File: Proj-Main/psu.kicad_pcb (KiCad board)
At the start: 2 copper layers, 100 x 75 mm, 126 parts, among them J1 METER, J3 T1A, J4 T1B, J5 T1C, J6 SENSE, J8 OUT+, J9 OUT-, Q1 BC856, Q10 BC856, Q11 PMP4201Y, Q12 MMBT3904, Q13 BC856, Q14 MMBT3904, Q15 PZT2222A, Q16 MMBT3904, Q17 TIP105, Q18 PMP4201Y, Q19 MMBT2907A, Q2 MMBT3904, Q20 MMBT2907A, Q21 MMBT2907A, Q22 MMBT3904, Q23 PMP4201Y, Q24 MMBT3904, Q3 PZT2222A, Q4 BC856, Q5 MMBT3906, Q6 MMBT3906, Q7 PMP4201Y, Q8 PMP4201Y, Q9 BC856

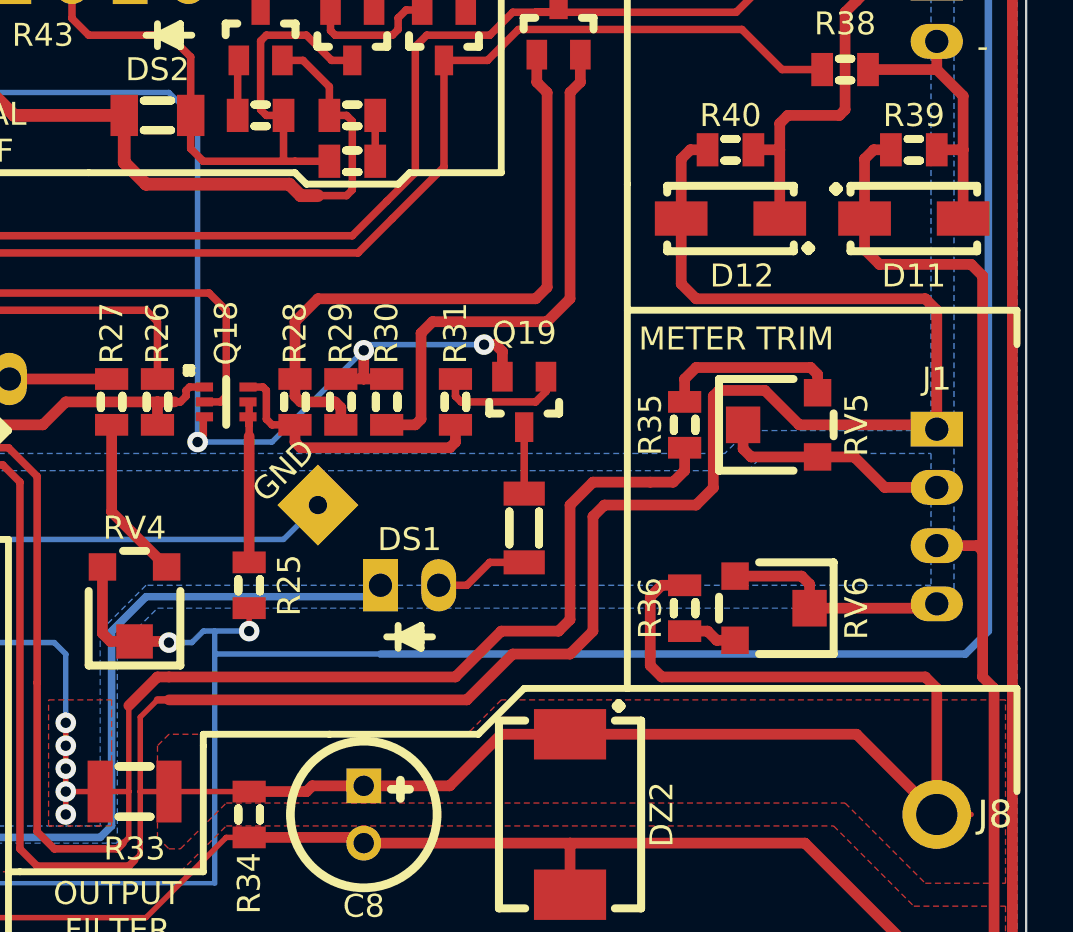
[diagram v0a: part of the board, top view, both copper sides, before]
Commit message: Rearranged schematic
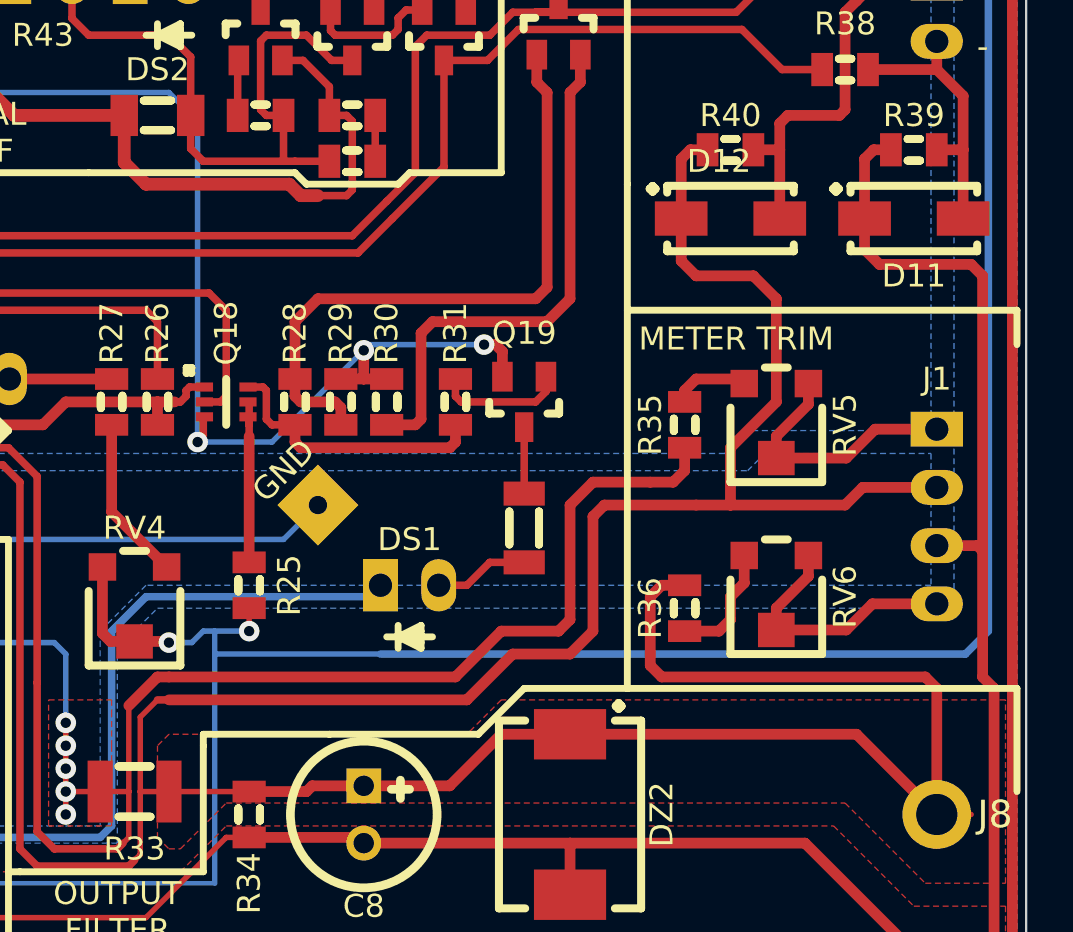
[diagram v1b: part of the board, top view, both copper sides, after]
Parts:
- moved RV6 0.50 mm to (214.0, 100.5), turned to 180 degrees
- turned D12 to 0 degrees
- turned RV5 to 180 degrees
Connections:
- D12 pad 1: Net-(D12-Pad1) -> /OUT+
- D12 pad 2: /OUT+ -> Net-(D12-Pad2)
- J1 pad 1: /OUT+ -> Net-(J1-Pad1)
- J1 pad 2: Net-(J1-Pad2) -> /OUT+
- J6 pad 1: Net-(D12-Pad1) -> Net-(D12-Pad2)
- R37 pad 1: Net-(D12-Pad1) -> Net-(D12-Pad2)
- R40 pad 2: Net-(D12-Pad1) -> Net-(D12-Pad2)
- RV5 pad 1: Net-(J1-Pad2) -> Net-(J1-Pad1)
- RV5 pad 2: Net-(J1-Pad2) -> Net-(J1-Pad1)
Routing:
- net Net-(D12-Pad2): track 0.00 -> 18.4 mm
- net Net-(D12-Pad1): track 18.4 -> 0.00 mm
- net Net-(J1-Pad1): track 0.00 -> 11.9 mm
- net Net-(J1-Pad2): track 10.2 -> 0.00 mm
- net /OUT+: track 195.2 -> 187.0 mm
- net Net-(R35-Pad2): track 7.93 -> 3.39 mm
- net Net-(R36-Pad2): track 2.37 -> 5.26 mm
- net Net-(J1-Pad4): track 10.3 -> 11.8 mm

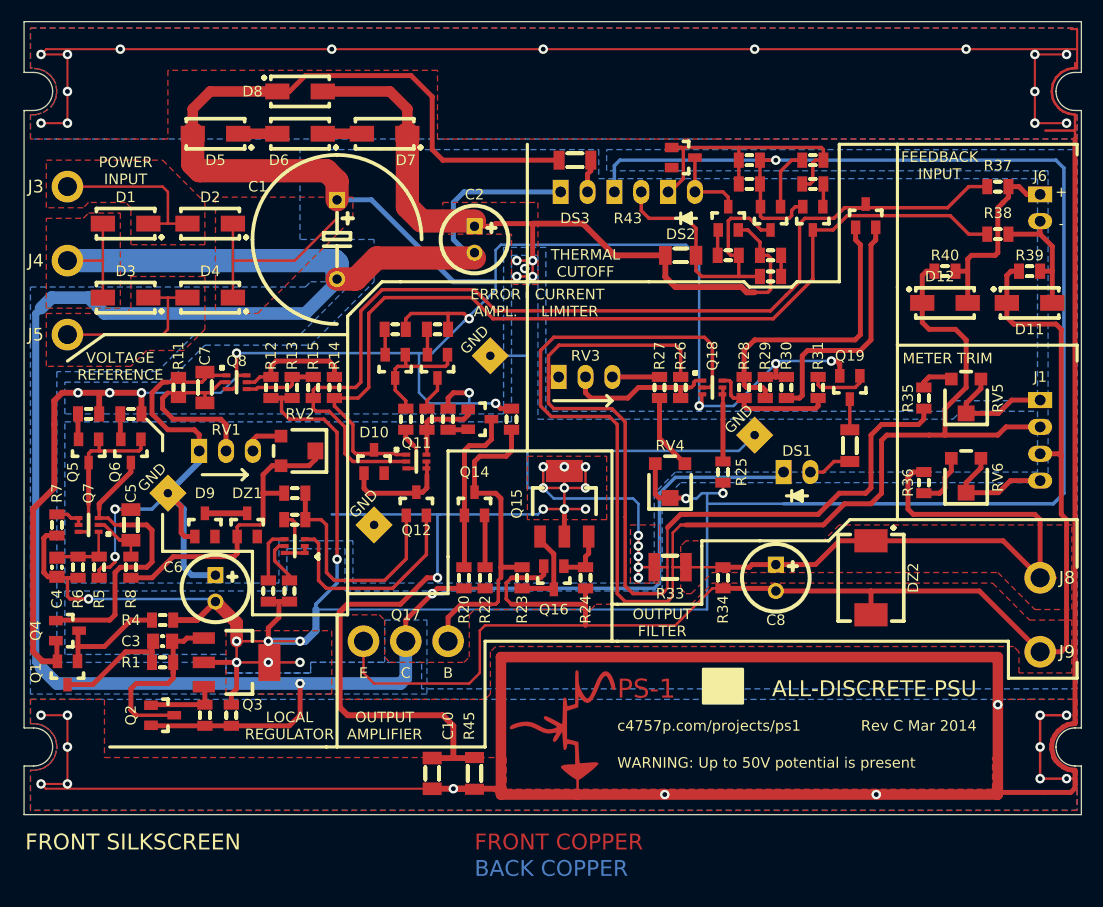
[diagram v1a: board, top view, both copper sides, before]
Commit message: Reannotated schematic
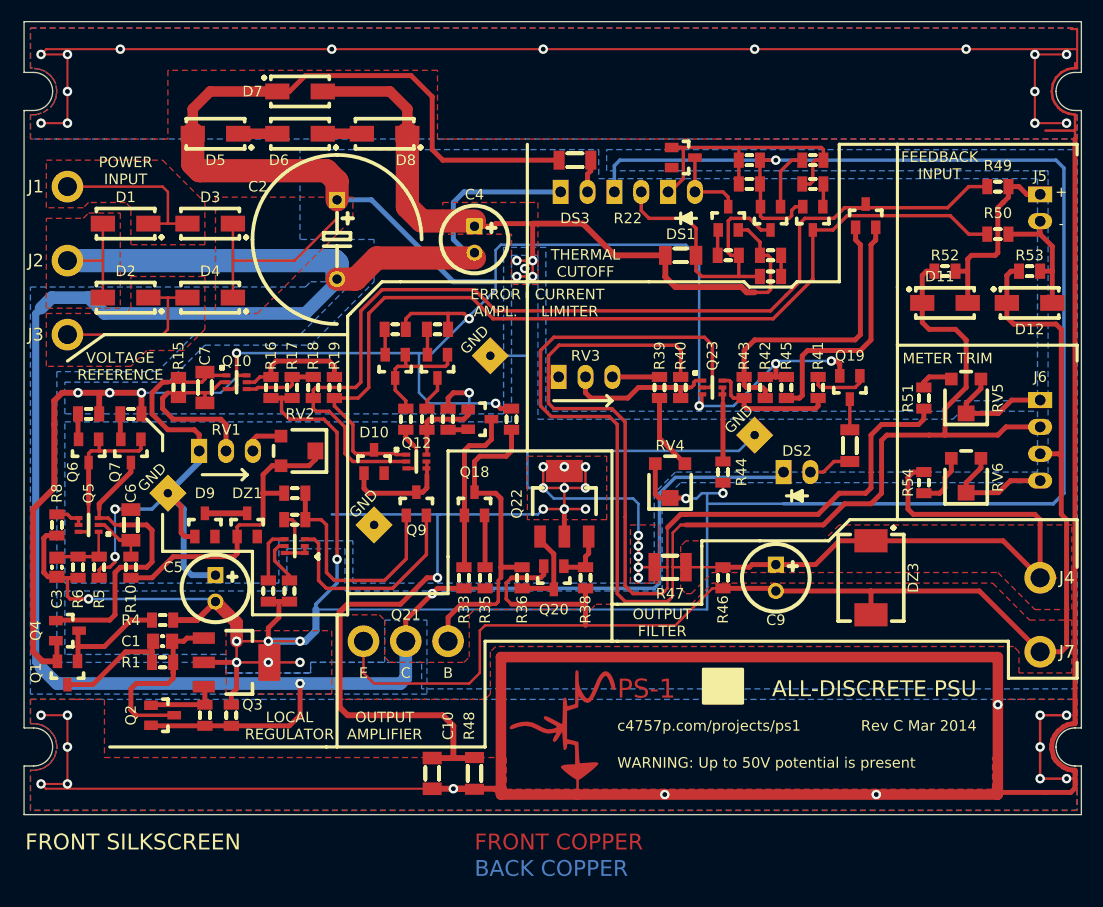
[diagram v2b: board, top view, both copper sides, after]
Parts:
- renumbered C3 to C1, C1 to C2, C4 to C3, C2 to C4, C6 to C5, C5 to C6, C9 to C8, C8 to C9, D12 to D11, D11 to D12, D3 to D2, D2 to D3, D8 to D7, D7 to D8, DS2 to DS1, DS1 to DS2, DZ3 to DZ2, DZ2 to DZ3, J3 to J1, J4 to J2, J5 to J3, J8 to J4, J6 to J5, J1 to J6, J9 to J7, Q8 to Q10, Q22 to Q11, Q11 to Q12, Q9 to Q13, Q21 to Q14, Q10 to Q15, Q24 to Q16, Q13 to Q17, Q14 to Q18, Q16 to Q20, Q17 to Q21, Q15 to Q22, Q18 to Q23, Q20 to Q24, Q7 to Q5, Q5 to Q6, Q6 to Q7, Q23 to Q8, Q12 to Q9, R8 to R10, R9 to R11, R10 to R12, R18 to R13, R49 to R14, R11 to R15, R12 to R16, R13 to R17, R15 to R18, R14 to R19, R3 to R2, R44 to R20, R50 to R21, R43 to R22, R54 to R23, R16 to R24, R42 to R25, R41 to R26, R51 to R27, R52 to R28, R55 to R29, R48 to R3, R17 to R30, R53 to R31, R19 to R32, R20 to R33, R21 to R34, R22 to R35, R23 to R36, R32 to R37, R24 to R38, R27 to R39, R26 to R40, R31 to R41, R29 to R42, R28 to R43, R25 to R44, R30 to R45, R34 to R46, R33 to R47, R45 to R48, R37 to R49, R38 to R50, R35 to R51, R40 to R52, R39 to R53, R36 to R54, R2 to R55, R46 to R7, R7 to R8, R47 to R9

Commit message: PCB tweaks
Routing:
- net CGND: track 404.7 -> 428.0 mm
- added copper zone on F.Cu, net +2
- removed copper zone on F.Cu, net V+
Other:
- board text added: "E100A"
- board text added: "May 2014"
- board text removed: "PS-1"
- board text removed: "Rev C Mar 2014"

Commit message: More PCB tweaks
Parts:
- moved R36 4.53 mm to (171.5, 105.5)
- moved Q6 2.50 mm to (129.0, 99.5)
- moved Q7 2.50 mm to (133.0, 99.5)
- moved R37 2.50 mm to (201.0, 96.0), turned to 180 degrees
- moved R7 2.50 mm to (129.0, 96.0)
- moved R9 2.50 mm to (133.0, 96.0)
- moved Q20 1.50 mm to (173.5, 110.0)
- moved R1 1.50 mm to (138.0, 119.5)
- moved C1 1.00 mm to (138.0, 117.0)
- moved R54 1.00 mm to (210.0, 100.0), turned to 90 degrees
- moved R13 0.56 mm to (150.5, 111.0)
- moved R4 0.50 mm to (138.0, 114.5)
- moved R51 0.50 mm to (210.0, 92.5)
- moved R14 0.25 mm to (148.0, 111.0)
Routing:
- net /OUT+: track 187.0 -> 180.2 mm
- net /OUT-: track 141.6 -> 138.2 mm
- net Net-(R36-Pad2): track 5.26 -> 2.72 mm
- net GND: track 367.5 -> 365.2 mm
- net Net-(Q4-Pad1): track 28.8 -> 26.5 mm
- net +2: track 273.1 -> 274.7 mm
- net Net-(Q15-Pad3): track 5.12 -> 6.62 mm
- net Net-(C3-Pad2): track 18.7 -> 17.2 mm
- net -12: track 279.0 -> 280.4 mm
- net Net-(Q5-Pad1): track 15.6 -> 14.6 mm
- net Net-(Q15-Pad1): track 9.32 -> 8.40 mm
- net Net-(Q23-Pad5): track 4.55 -> 5.35 mm
- net Net-(DS2-PadK): track 29.0 -> 29.8 mm
- net Net-(C3-Pad1): track 11.5 -> 10.9 mm

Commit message: PCB and rendering tweaks
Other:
- board text added: "c4757p.com/projects/e100a"
- board text removed: "c4757p.com/projects/ps1"

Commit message: Zone under Q3 was assigned to the wrong net
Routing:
- added copper zone on F.Cu, net -12
- removed copper zone on F.Cu, net V-

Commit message: Frequency compensation
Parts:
- removed R21: 1k, IPC7351-Nominal:RESC2012X50
- added C11: 1n, IPC7351-Nominal:CAPC2012X70, F.Cu at (156.5, 95.0)
- added C12: 330p, IPC7351-Nominal:CAPC2012X70, F.Cu at (187.0, 95.5)
- added R56: 1k, IPC7351-Nominal:RESC2012X50, F.Cu at (158.8, 95.0)
- added R57: 1k, IPC7351-Nominal:RESC2012X50, F.Cu at (190.5, 95.5)
- C1: value 100p -> 330p
- R20, R42: value 1k -> 2k
- R45: value 33 -> 1k
- moved TP3 1.25 mm to (195.2, 96.5)
- moved R23 1.12 mm to (159.0, 86.0), turned to 270 degrees
- moved R29 1.12 mm to (163.0, 86.0), turned to 270 degrees
- moved RV2 0.71 mm to (150.5, 98.5)
- turned R20 to 180 degrees
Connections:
- C8 pad 2: Net-(C9-Pad2) -> Net-(C8-Pad2)
- Q11 pad 3: Net-(C9-Pad2) -> Net-(C8-Pad2)
- R20 pad 2: Net-(R44-Pad2) -> Net-(C8-Pad2)
- R22 pad 2: Net-(C9-Pad2) -> Net-(C8-Pad2)
- R25 pad 2: Net-(C9-Pad2) -> Net-(C8-Pad2)
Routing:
- net Net-(C11-Pad2): track 31.4 -> 62.6 mm
- net Net-(C9-Pad2): track 28.7 -> 0.00 mm
- net Net-(C8-Pad2): track 0.00 -> 27.3 mm
- net Net-(C11-Pad1): track 0.00 -> 3.83 mm
- net Net-(Q23-Pad6): track 12.2 -> 15.2 mm
- net Net-(C12-Pad2): track 14.6 -> 17.5 mm
- net /FB-: track 90.2 -> 92.4 mm
- net Net-(R44-Pad2): track 2.00 -> 0.00 mm
- net Net-(C12-Pad1): track 0.00 -> 1.60 mm
- net Net-(RV1-Pad3): track 3.85 -> 2.53 mm
- net /FB+: track 95.8 -> 94.8 mm
- net -12: track 280.4 -> 279.4 mm
- net +2: track 274.7 -> 273.9 mm
- net Net-(Q15-Pad2): track 2.42 -> 1.92 mm
- net Net-(Q13-Pad2): track 2.42 -> 1.92 mm
- added copper zone on F.Cu, net Net-(D3-Pad1)
- removed copper zone on F.Cu, net Net-(D2-Pad1)

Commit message: Fixed another disconnected zone
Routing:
- added copper zone on F.Cu, net Net-(D2-Pad1)
- removed copper zone on F.Cu, net Net-(D3-Pad1)
